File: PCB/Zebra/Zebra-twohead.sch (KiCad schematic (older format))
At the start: 9 parts, among them J1 Conn_01x11, J2 MJ-4PP-9, U1 ProMicro, U2 ssd1306

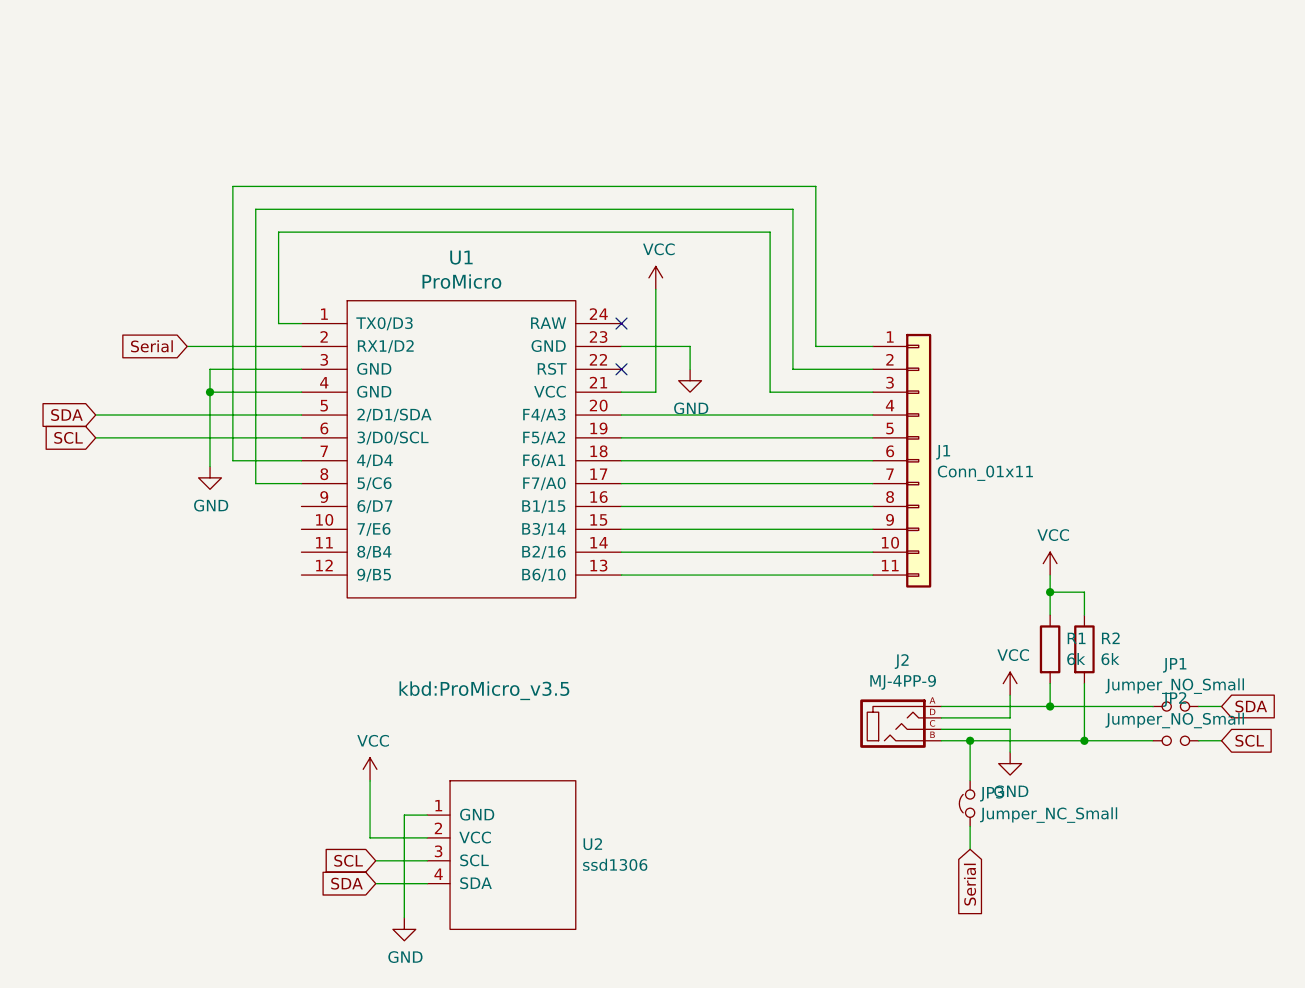
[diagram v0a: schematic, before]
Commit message: Add extra connector, LED, clean up
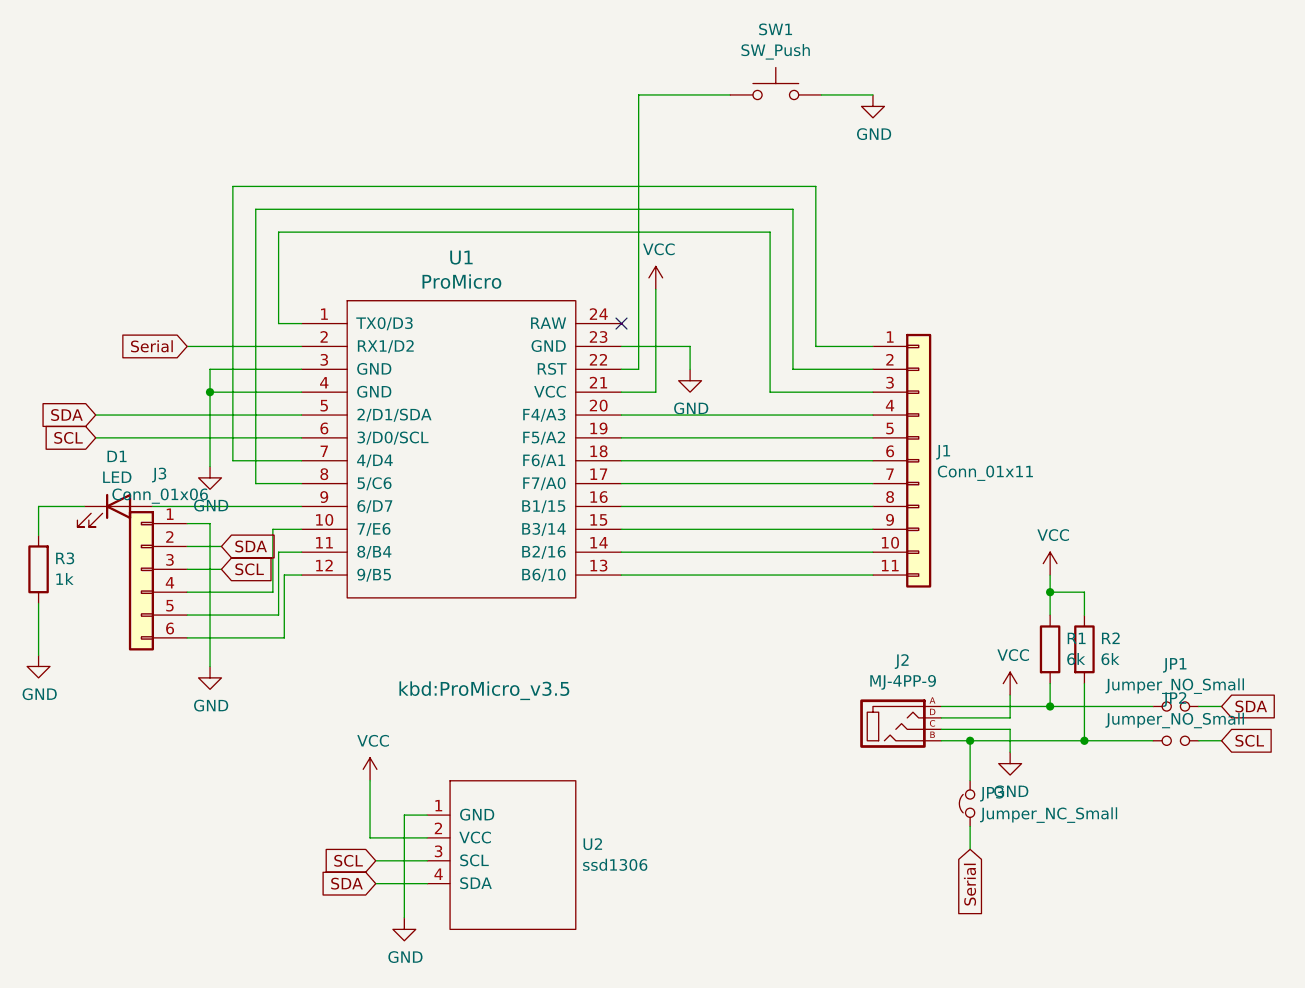
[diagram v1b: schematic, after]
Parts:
- added D1: LED, LED_THT:LED_D3.0mm, symbol Device:LED
- added J3: Conn_01x06, Connector_PinHeader_2.54mm:PinHeader_1x06_P2.54mm_Vertical, symbol Connector_Generic:Conn_01x06
- added R3: 1k, Resistor_SMD:R_1206_3216Metric_Pad1.30x1.75mm_HandSolder, symbol Device:R
- added SW1: SW_Push, kbd:ResetSW_1side, symbol Switch:SW_Push
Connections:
- net GND: now also J3.1 (Pin_1), R3.1, SW1.2
- net SCL: now also J3.3 (Pin_3)
- net SDA: now also J3.2 (Pin_2)
- net at U1.10 (7/E6): now also J3.4 (Pin_4)
- net at U1.11 (8/B4): now also J3.5 (Pin_5)
- net at U1.12 (9/B5): now also J3.6 (Pin_6)
- net at U1.22 (RST): now also SW1.1
- net at U1.9 (6/D7): now also D1.2 (A)
- new net: D1.1 (K), R3.2
- no-connect marks 2 -> 1
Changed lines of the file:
@@
 	2200 4650 2200 5100
 NoConn ~ 3150 2500
-NoConn ~ 3150 2700
 Wire Wire Line
 	1550 3200 1750 3200
@@
 Text GLabel 850  2900 0    50   Input ~ 0
 SDA
-Text GLabel 850  3000 0    50   Input ~ 0
-SCL
 Wire Wire Line
 	1750 2900 850  2900
@@
 Wire Wire Line
 	5175 4325 5475 4325
+$Comp
+L Device:LED D1
+U 1 1 5FD7814F
+P 950 3300
+F 0 "D1" H 943 3517 50  0000 C CNN
+F 1 "LED" H 943 3426 50  0000 C CNN
+F 2 "LED_THT:LED_D3.0mm" H 950 3300 50  0001 C CNN
+F 3 "~" H 950 3300 50  0001 C CNN
+	1    950  3300
+	1    0    0    -1
+$EndComp
+$Comp
+L Device:R R3
+U 1 1 5FD7949A
+P 600 3575
+F 0 "R3" H 530 3529 50  0000 R CNN
+F 1 "1k" H 530 3620 50  0000 R CNN
+F 2 "Resistor_SMD:R_1206_3216Metric_Pad1.30x1.75mm_HandSolder" V 530 3575 50  0001 C CNN
+F 3 "~" H 600 3575 50  0001 C CNN
+	1    600  3575
+	-1   0    0    1
+$EndComp
+Wire Wire Line
+	1750 3300 1100 3300
+Wire Wire Line
+	800  3300 600  3300
+Wire Wire Line
+	600  3300 600  3425
+$Comp
+L power:GND #PWR0104
+U 1 1 5FD7D569
+P 600 3950
+F 0 "#PWR0104" H 600 3700 50  0001 C CNN
+F 1 "GND" H 605 3777 50  0000 C CNN
+F 2 "" H 600 3950 50  0001 C CNN
+F 3 "" H 600 3950 50  0001 C CNN
+	1    600  3950
+	1    0    0    -1
+$EndComp
+Wire Wire Line
+	600  3725 600  3950
+$Comp
+L Connector_Generic:Conn_01x06 J3
+U 1 1 5FD7FCEF
+P 1050 3575
+F 0 "J3" H 968 3992 50  0000 C CNN
+F 1 "Conn_01x06" H 968 3901 50  0000 C CNN
+F 2 "Connector_PinHeader_2.54mm:PinHeader_1x06_P2.54mm_Vertical" H 1050 3575 50  0001 C CNN
+F 3 "~" H 1050 3575 50  0001 C CNN
+	1    1050 3575
+	-1   0    0    -1
+$EndComp
+$Comp
+L power:GND #PWR0105
+U 1 1 5FD84F14
+P 1350 4000
+F 0 "#PWR0105" H 1350 3750 50  0001 C CNN
+F 1 "GND" H 1355 3827 50  0000 C CNN
+F 2 "" H 1350 4000 50  0001 C CNN
+F 3 "" H 1350 4000 50  0001 C CNN
+	1    1350 4000
+	1    0    0    -1
+$EndComp
+Text GLabel 1400 3475 2    50   Input ~ 0
+SDA
+Text GLabel 850  3000 0    50   Input ~ 0
+SCL
+Text GLabel 1400 3575 2    50   Input ~ 0
+SCL
+$Comp
+L Switch:SW_Push SW1
+U 1 1 5FD8D75C
+P 3825 1500
+F 0 "SW1" H 3825 1785 50  0000 C CNN
+F 1 "SW_Push" H 3825 1694 50  0000 C CNN
+F 2 "kbd:ResetSW_1side" H 3825 1700 50  0001 C CNN
+F 3 "~" H 3825 1700 50  0001 C CNN
+	1    3825 1500
+	1    0    0    -1
+$EndComp
+Wire Wire Line
+	3225 2700 3225 1500
+Wire Wire Line
+	3225 1500 3625 1500
+Wire Wire Line
+	3150 2700 3225 2700
+$Comp
+L power:GND #PWR0106
+U 1 1 5FD94DA7
+P 4250 1500
+F 0 "#PWR0106" H 4250 1250 50  0001 C CNN
+F 1 "GND" H 4255 1327 50  0000 C CNN
+F 2 "" H 4250 1500 50  0001 C CNN
+F 3 "" H 4250 1500 50  0001 C CNN
+	1    4250 1500
+	1    0    0    -1
+$EndComp
+Wire Wire Line
+	4025 1500 4250 1500
+Wire Wire Line
+	1250 3375 1350 3375
+Wire Wire Line
+	1350 3375 1350 4000
+Wire Wire Line
+	1400 3475 1250 3475
+Wire Wire Line
+	1250 3575 1400 3575
+Wire Wire Line
+	1750 3400 1625 3400
+Wire Wire Line
+	1750 3500 1650 3500
+Wire Wire Line
+	1750 3600 1675 3600
+Wire Wire Line
+	1625 3400 1625 3675
+Wire Wire Line
+	1625 3675 1250 3675
+Wire Wire Line
+	1650 3500 1650 3775
+Wire Wire Line
+	1650 3775 1250 3775
+Wire Wire Line
+	1675 3600 1675 3875
+Wire Wire Line
+	1675 3875 1250 3875
 $EndSCHEMATC
